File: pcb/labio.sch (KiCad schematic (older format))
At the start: 0 parts

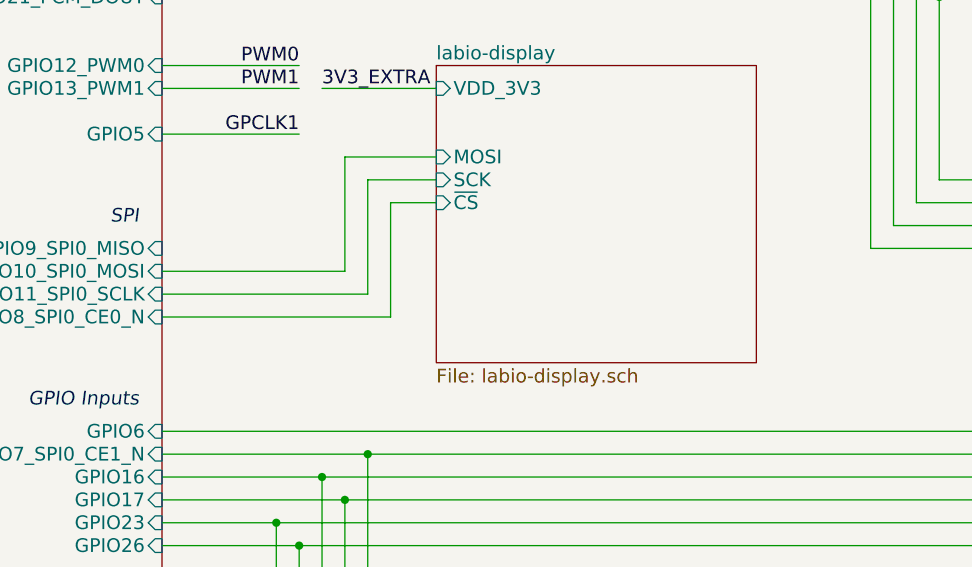
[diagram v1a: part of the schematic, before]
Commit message: using MISO/gpio for D/C on led screen and layout. bump to rev 1.2.0.
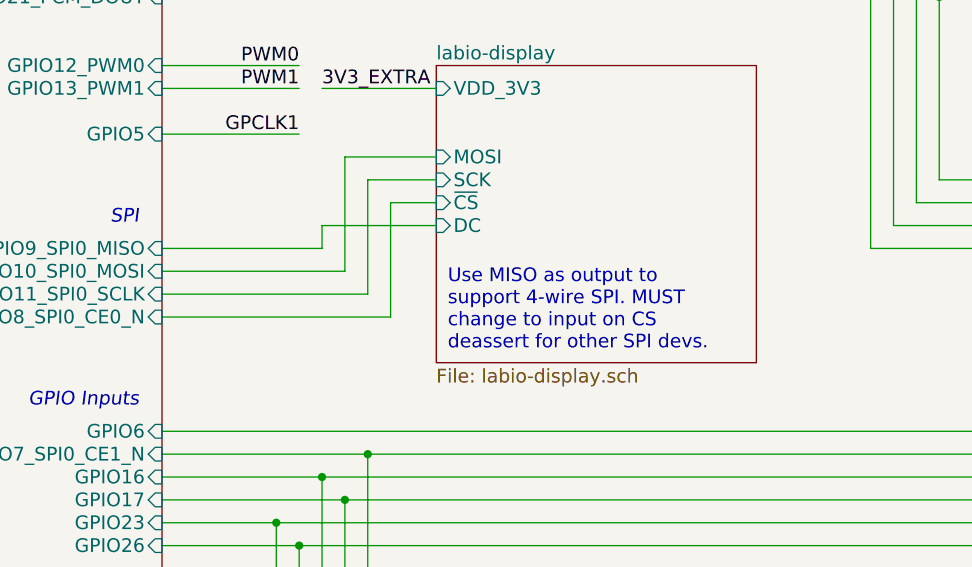
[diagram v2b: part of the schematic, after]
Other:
- note added: "Use MISO as output to\nsupport 4-wire SPI. MUST\nchange to input on CS\ndeassert for other SPI devs."
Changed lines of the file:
@@
 Title "Raspberry Pi Embedded Lab I/O"
 Date ""
-Rev "1.1.4"
+Rev "1.2.0"
 Comp "Carnegie Mellon University"
 Comment1 ""
@@
 F4 "SCK" I L 3700 3900 60
 F5 "MOSI" I L 3700 3800 60
+F6 "DC" I L 3700 4100 60
 $EndSheet
 $Sheet
@@
 F1 "labio-mech.sch" 60
 $EndSheet
+Wire Wire Line
+	2500 4200 3200 4200
+Wire Wire Line
+	3200 4200 3200 4100
+Wire Wire Line
+	3200 4100 3700 4100
+Text Notes 3750 4650 0    60   ~ 0
+Use MISO as output to\nsupport 4-wire SPI. MUST\nchange to input on CS\ndeassert for other SPI devs.
 $EndSCHEMATC

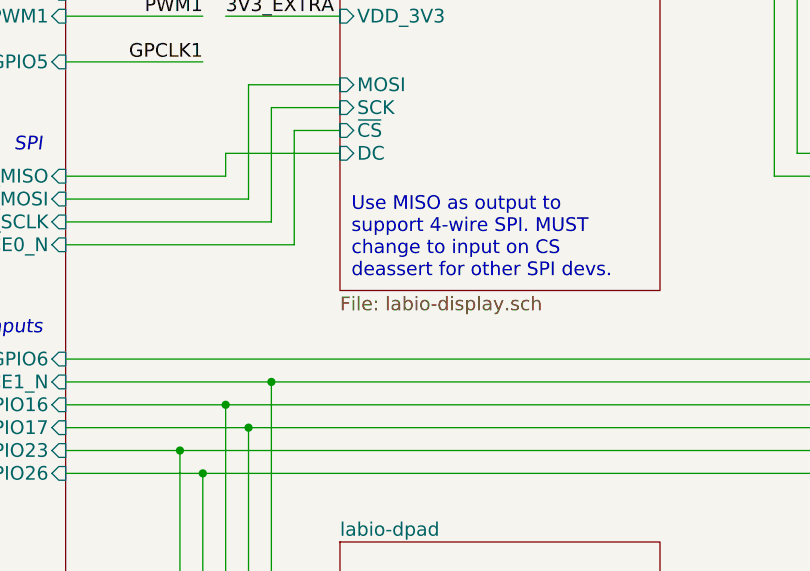
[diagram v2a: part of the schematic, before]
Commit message: add options for driving oled reset. no changes to stuffed bom parts.
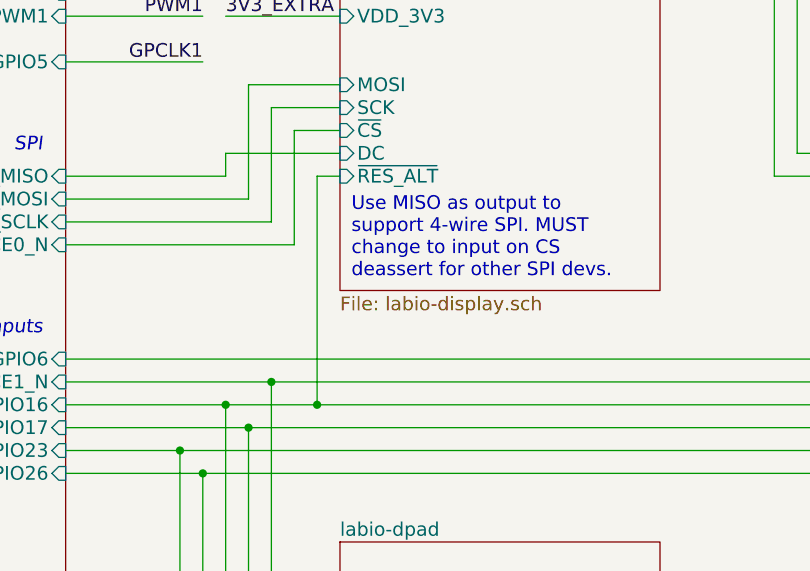
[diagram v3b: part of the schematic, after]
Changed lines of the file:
@@
 F5 "MOSI" I L 3700 3800 60
 F6 "DC" I L 3700 4100 60
+F7 "~RES_ALT" I L 3700 4200 60
 $EndSheet
 $Sheet
@@
 Text Notes 3750 4650 0    60   ~ 0
 Use MISO as output to\nsupport 4-wire SPI. MUST\nchange to input on CS\ndeassert for other SPI devs.
+Wire Wire Line
+	3700 4200 3600 4200
+Wire Wire Line
+	3600 4200 3600 5200
+Connection ~ 3600 5200
 $EndSCHEMATC
